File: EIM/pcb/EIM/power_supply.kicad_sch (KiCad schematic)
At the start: 18 parts, among them U2 AP63203WU, U6 AP63200WU

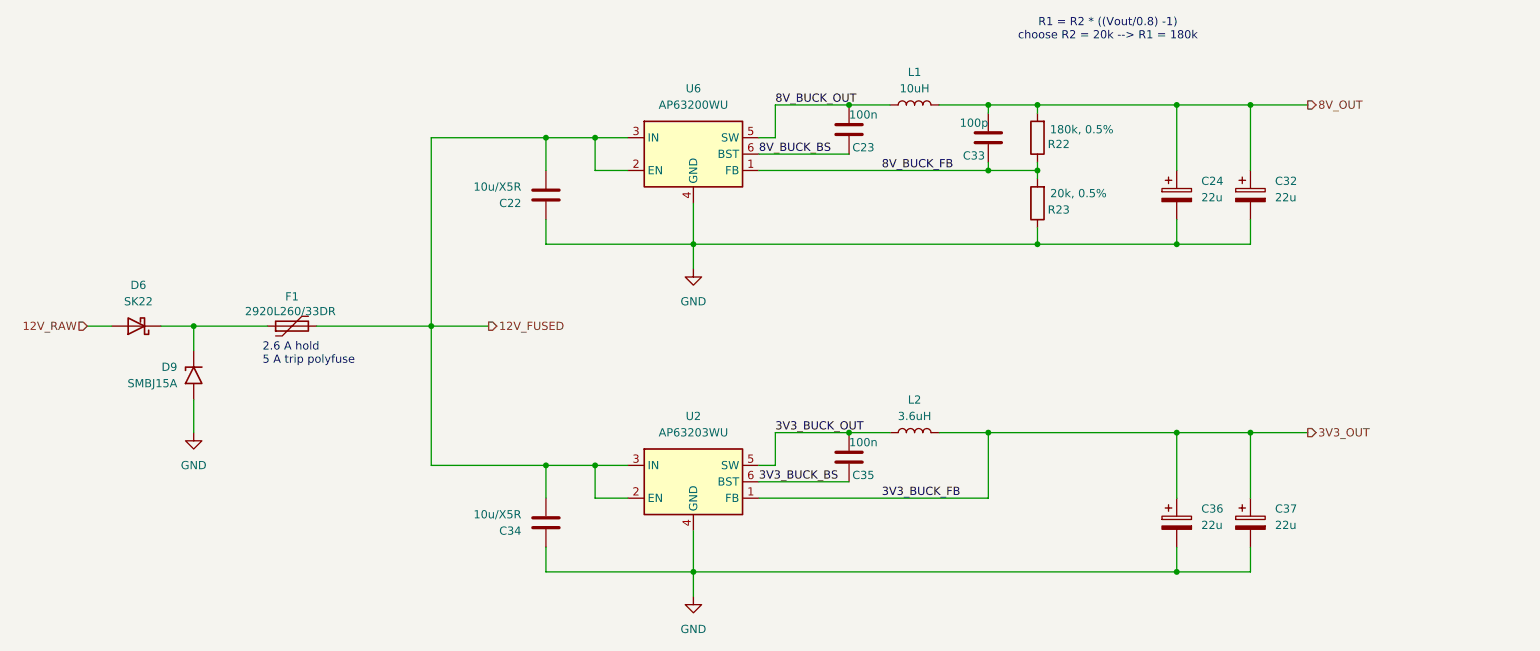
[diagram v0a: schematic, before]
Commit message: added Arjun's comments, assigned some MCU pins
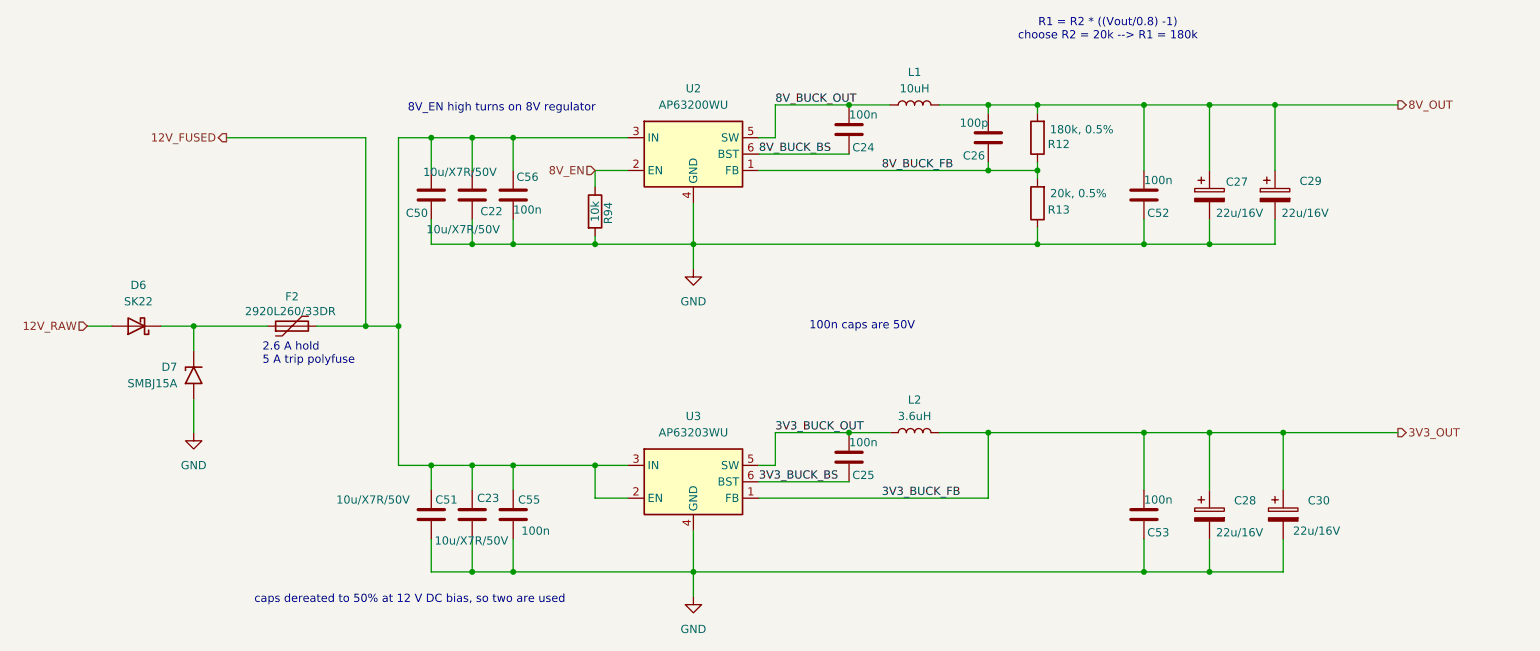
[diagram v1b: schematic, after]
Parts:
- added C50, C51: 10u/X7R/50V, Capacitor_SMD:C_1206_3216Metric_Pad1.33x1.80mm_HandSolder, symbol Device:C
- added C52, C53, C55, C56: 100n, Capacitor_SMD:C_0805_2012Metric_Pad1.18x1.45mm_HandSolder, symbol Device:C
- added R94: 10k, Resistor_SMD:R_0805_2012Metric_Pad1.20x1.40mm_HandSolder, symbol Device:R
- C22: value 10u/X5R -> 10u/X7R/50V
- C23: renamed from C34; value 10u/X5R -> 10u/X7R/50V
- C27: renamed from C24; value 22u -> 22u/16V
- C28: renamed from C36; value 22u -> 22u/16V
- C29: renamed from C32; value 22u -> 22u/16V
- C30: renamed from C37; value 22u -> 22u/16V
- renumbered C23 to C24, C35 to C25, C33 to C26, D9 to D7, F1 to F2, R22 to R12, R23 to R13, U6 to U2, U2 to U3
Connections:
- net 12V_FUSED: now also C50.1, C51.2, C55.1, C56.2; no longer U2.2 (EN)
- net 3V3_OUT: now also C53.1
- net 8V_OUT: now also C52.1
- net GND: now also C50.2, C51.1, C52.2, C53.2, C55.2, C56.1, R94.2
- new net 8V_EN: R94.1, U2.2 (EN)
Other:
- note added: "100n caps are 50V"
- note added: "8V_EN high turns on 8V regulator"
- note added: "caps dereated to 50% at 12 V DC bias, so two are used"
- moved on the sheet: C22, C23, C27, C28, C29, C30

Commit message: Layout 75% done, before 8V bus deletion
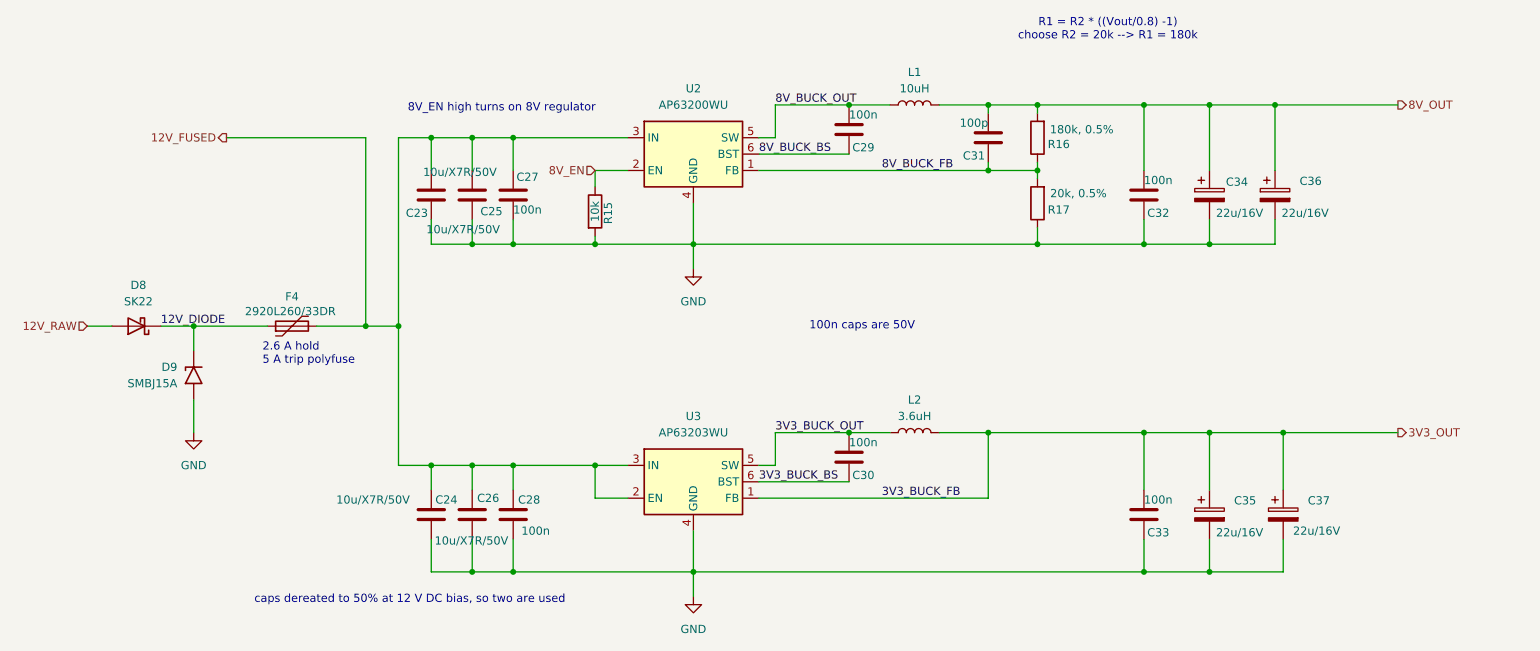
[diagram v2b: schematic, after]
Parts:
- renumbered C50 to C23, C51 to C24, C22 to C25, C23 to C26, C56 to C27, C55 to C28, C24 to C29, C25 to C30, C26 to C31, C52 to C32, C53 to C33, C27 to C34, C28 to C35, C29 to C36, C30 to C37, D6 to D8, D7 to D9, F2 to F4, R94 to R15, R12 to R16, R13 to R17
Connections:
- net 12V_DIODE: now reaches D8.1 (K), D9.1 (A1), F4.1
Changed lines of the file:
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@@
+		)
+	)
+	(label "12V_DIODE"
+		(at 50.8 95.25 0)
+		(fields_autoplaced yes)
+		(effects
+			(font
+				(size 1.27 1.27)
+			)
+			(justify left bottom)
 		)
 	)
@@
 		(on_board yes)
 		(dnp no)
-		(property "Reference" "C55"
+		(property "Reference" "C28"
 			(at 106.172 122.174 0)
 			(effects
@@
 			(project "EIM"
 				(path "/2e0b3b3d-5537-41dc-9fad-4fb33afdbfad/dc39c068-2af2-4b70-9a5c-946b676fc222"
-					(reference "C55")
+					(reference "C28")
 					(unit 1)
 				)
@@
 		(on_board yes)
 		(dnp no)
-		(property "Reference" "C50"
+		(property "Reference" "C23"
 			(at 92.202 77.724 0)
 			(effects
@@
 			(project "EIM"
 				(path "/2e0b3b3d-5537-41dc-9fad-4fb33afdbfad/dc39c068-2af2-4b70-9a5c-946b676fc222"
-					(reference "C50")
+					(reference "C23")
 					(unit 1)
 				)
@@
 		(on_board yes)
 		(dnp no)
-		(property "Reference" "C56"
+		(property "Reference" "C27"
 			(at 105.918 72.136 0)
 			(effects
@@
 			(project "EIM"
 				(path "/2e0b3b3d-5537-41dc-9fad-4fb33afdbfad/dc39c068-2af2-4b70-9a5c-946b676fc222"
-					(reference "C56")
+					(reference "C27")
 					(unit 1)
 				)
@@
 		(on_board yes)
 		(dnp no)
-		(property "Reference" "C26"
+		(property "Reference" "C31"
 			(at 178.562 68.834 0)
 			(effects
@@
 			(project "EIM"
 				(path "/2e0b3b3d-5537-41dc-9fad-4fb33afdbfad/dc39c068-2af2-4b70-9a5c-946b676fc222"
-					(reference "C26")
+					(reference "C31")
 					(unit 1)
 				)
@@
 		(on_board yes)
 		(dnp no)
-		(property "Reference" "C28"
+		(property "Reference" "C35"
 			(at 217.17 122.3009 0)
 			(effects
@@
 			(project "EIM"
 				(path "/2e0b3b3d-5537-41dc-9fad-4fb33afdbfad/dc39c068-2af2-4b70-9a5c-946b676fc222"
-					(reference "C28")
+					(reference "C35")
 					(unit 1)
 				)
@@
 		(on_board yes)
 		(dnp no)
-		(property "Reference" "R94"
+		(property "Reference" "R15"
 			(at 120.142 77.724 90)
 			(effects
@@
 			(project "EIM"
 				(path "/2e0b3b3d-5537-41dc-9fad-4fb33afdbfad/dc39c068-2af2-4b70-9a5c-946b676fc222"
-					(reference "R94")
+					(reference "R15")
 					(unit 1)
 				)
@@
 		(on_board yes)
 		(dnp no)
-		(property "Reference" "C24"
+		(property "Reference" "C29"
 			(at 157.988 67.564 0)
 			(effects
@@
 			(project "EIM"
 				(path "/2e0b3b3d-5537-41dc-9fad-4fb33afdbfad/dc39c068-2af2-4b70-9a5c-946b676fc222"
-					(reference "C24")
+					(reference "C29")
 					(unit 1)
 				)
@@
 		(on_board yes)
 		(dnp no)
-		(property "Reference" "C29"
+		(property "Reference" "C36"
 			(at 227.33 72.7709 0)
 			(effects
@@
 			(project "EIM"
 				(path "/2e0b3b3d-5537-41dc-9fad-4fb33afdbfad/dc39c068-2af2-4b70-9a5c-946b676fc222"
-					(reference "C29")
+					(reference "C36")
 					(unit 1)
 				)
@@
 		(on_board yes)
 		(dnp no)
-		(property "Reference" "C52"
+		(property "Reference" "C32"
 			(at 203.708 77.724 0)
 			(effects
@@
 			(project "EIM"
 				(path "/2e0b3b3d-5537-41dc-9fad-4fb33afdbfad/dc39c068-2af2-4b70-9a5c-946b676fc222"
-					(reference "C52")
+					(reference "C32")
 					(unit 1)
 				)
@@
 		(on_board yes)
 		(dnp no)
-		(property "Reference" "C25"
+		(property "Reference" "C30"
 			(at 157.988 118.364 0)
 			(effects
@@
 			(project "EIM"
 				(path "/2e0b3b3d-5537-41dc-9fad-4fb33afdbfad/dc39c068-2af2-4b70-9a5c-946b676fc222"
-					(reference "C25")
+					(reference "C30")
 					(unit 1)
 				)
@@
 		(dnp no)
 		(fields_autoplaced yes)
-		(property "Reference" "#PWR067"
+		(property "Reference" "#PWR076"
 			(at 133.35 143.51 0)
 			(effects
@@
 			(project "EIM"
 				(path "/2e0b3b3d-5537-41dc-9fad-4fb33afdbfad/dc39c068-2af2-4b70-9a5c-946b676fc222"
-					(reference "#PWR067")
+					(reference "#PWR076")
 					(unit 1)
 				)
@@
 		(dnp no)
 		(fields_autoplaced yes)
-		(property "Reference" "D6"
+		(property "Reference" "D8"
 			(at 47.3075 88.9 0)
 			(effects
@@
 			(project ""
 				(path "/2e0b3b3d-5537-41dc-9fad-4fb33afdbfad/dc39c068-2af2-4b70-9a5c-946b676fc222"
-					(reference "D6")
+					(reference "D8")
 					(unit 1)
 				)
@@
 		(dnp no)
 		(fields_autoplaced yes)
-		(property "Reference" "#PWR066"
+		(property "Reference" "#PWR075"
 			(at 133.35 92.71 0)
 			(effects
@@
 			(project "EIM"
 				(path "/2e0b3b3d-5537-41dc-9fad-4fb33afdbfad/dc39c068-2af2-4b70-9a5c-946b676fc222"
-					(reference "#PWR066")
+					(reference "#PWR075")
 					(unit 1)
 				)
@@
 		(on_board yes)
 		(dnp no)
-		(property "Reference" "C51"
+		(property "Reference" "C24"
 			(at 96.774 122.174 0)
 			(effects
@@
 			(project "EIM"
 				(path "/2e0b3b3d-5537-41dc-9fad-4fb33afdbfad/dc39c068-2af2-4b70-9a5c-946b676fc222"
-					(reference "C51")
+					(reference "C24")
 					(unit 1)
 				)
@@
 		(on_board yes)
 		(dnp no)
-		(property "Reference" "D7"
+		(property "Reference" "D9"
 			(at 53.34 101.5999 90)
 			(effects
@@
 			(project "EIM"
 				(path "/2e0b3b3d-5537-41dc-9fad-4fb33afdbfad/dc39c068-2af2-4b70-9a5c-946b676fc222"
-					(reference "D7")
+					(reference "D9")
 					(unit 1)
 				)
@@
 		(on_board yes)
 		(dnp no)
-		(property "Reference" "C22"
+		(property "Reference" "C25"
 			(at 100.33 77.47 0)
 			(effects
@@
 			(project "EIM"
 				(path "/2e0b3b3d-5537-41dc-9fad-4fb33afdbfad/dc39c068-2af2-4b70-9a5c-946b676fc222"
-					(reference "C22")
+					(reference "C25")
 					(unit 1)
 				)
@@
 		(on_board yes)
 		(dnp no)
-		(property "Reference" "C30"
+		(property "Reference" "C37"
 			(at 228.6 122.3009 0)
 			(effects
@@
 			(project "EIM"
 				(path "/2e0b3b3d-5537-41dc-9fad-4fb33afdbfad/dc39c068-2af2-4b70-9a5c-946b676fc222"
-					(reference "C30")
+					(reference "C37")
 					(unit 1)
 				)
@@
 		(on_board yes)
 		(dnp no)
-		(property "Reference" "C53"
+		(property "Reference" "C33"
 			(at 203.708 127.254 0)
 			(effects
@@
 			(project "EIM"
 				(path "/2e0b3b3d-5537-41dc-9fad-4fb33afdbfad/dc39c068-2af2-4b70-9a5c-946b676fc222"
-					(reference "C53")
+					(reference "C33")
 					(unit 1)
 				)
@@
 		(dnp no)
 		(fields_autoplaced yes)
-		(property "Reference" "#PWR065"
+		(property "Reference" "#PWR074"
 			(at 55.88 118.11 0)
 			(effects
@@
 			(project "EIM"
 				(path "/2e0b3b3d-5537-41dc-9fad-4fb33afdbfad/dc39c068-2af2-4b70-9a5c-946b676fc222"
-					(reference "#PWR065")
+					(reference "#PWR074")
 					(unit 1)
 				)
@@
 		(on_board yes)
 		(dnp no)
-		(property "Reference" "R12"
+		(property "Reference" "R16"
 			(at 189.992 67.056 0)
 			(effects
@@
 			(project "EIM"
 				(path "/2e0b3b3d-5537-41dc-9fad-4fb33afdbfad/dc39c068-2af2-4b70-9a5c-946b676fc222"
-					(reference "R12")
+					(reference "R16")
 					(unit 1)
 				)
@@
 		(on_board yes)
 		(dnp no)
-		(property "Reference" "F2"
+		(property "Reference" "F4"
 			(at 71.12 90.678 90)
 			(effects
@@
 			(project "EIM"
 				(path "/2e0b3b3d-5537-41dc-9fad-4fb33afdbfad/dc39c068-2af2-4b70-9a5c-946b676fc222"
-					(reference "F2")
+					(reference "F4")
 					(unit 1)
 				)
@@
 		(on_board yes)
 		(dnp no)
-		(property "Reference" "C27"
+		(property "Reference" "C34"
 			(at 215.9 72.898 0)
 			(effects
@@
 			(project ""
 				(path "/2e0b3b3d-5537-41dc-9fad-4fb33afdbfad/dc39c068-2af2-4b70-9a5c-946b676fc222"
-					(reference "C27")
+					(reference "C34")
 					(unit 1)
 				)
@@
 		(on_board yes)
 		(dnp no)
-		(property "Reference" "R13"
+		(property "Reference" "R17"
 			(at 189.992 77.216 0)
 			(effects
@@
 			(project "EIM"
 				(path "/2e0b3b3d-5537-41dc-9fad-4fb33afdbfad/dc39c068-2af2-4b70-9a5c-946b676fc222"
-					(reference "R13")
+					(reference "R17")
 					(unit 1)
 				)
@@
 		(on_board yes)
 		(dnp no)
-		(property "Reference" "C23"
+		(property "Reference" "C26"
 			(at 99.822 121.92 0)
 			(effects
@@
 			(project "EIM"
 				(path "/2e0b3b3d-5537-41dc-9fad-4fb33afdbfad/dc39c068-2af2-4b70-9a5c-946b676fc222"
-					(reference "C23")
-					(unit 1)
-				)
+					(reference "C26")
+					(unit 1)
+				)

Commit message: All components placed and pins assigned.
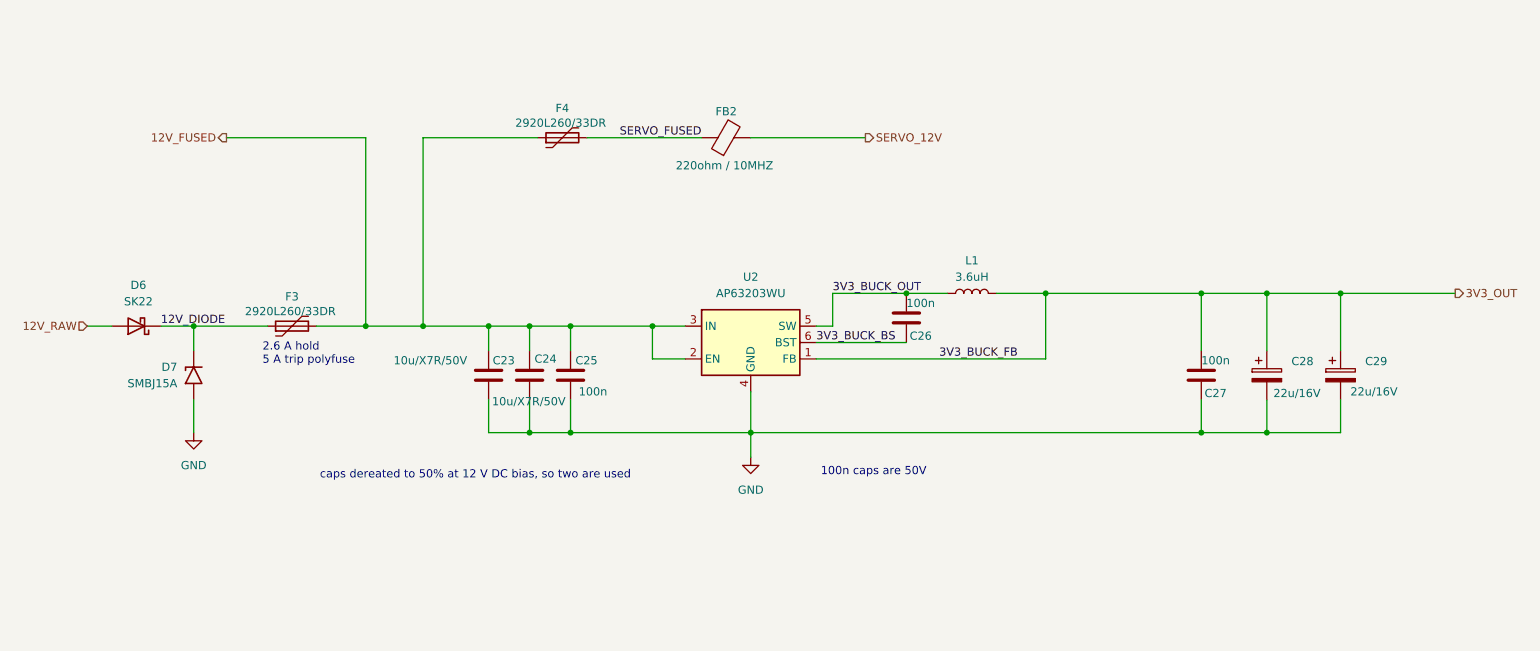
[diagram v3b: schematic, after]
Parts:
- removed C23, C25: 10u/X7R/50V, Capacitor_SMD:C_1206_3216Metric_Pad1.33x1.80mm_HandSolder, symbol Device:C
- removed C27, C29, C32: 100n, Capacitor_SMD:C_0805_2012Metric_Pad1.18x1.45mm_HandSolder, symbol Device:C
- removed C31: 100p, Capacitor_SMD:C_0805_2012Metric_Pad1.18x1.45mm_HandSolder, symbol Device:C
- removed C34, C36: 22u/16V, Capacitor_SMD:CP_Elec_4x5.8, symbol Device:C_Polarized
- removed L1: 10uH, Inductor_SMD:L_Bourns-SRN8040_8x8.15mm, symbol Device:L
- removed R15: 10k, Resistor_SMD:R_0805_2012Metric_Pad1.20x1.40mm_HandSolder, symbol Device:R
- removed R16: 180k, 0.5%, Resistor_SMD:R_0805_2012Metric_Pad1.20x1.40mm_HandSolder, symbol Device:R
- removed R17: 20k, 0.5%, Resistor_SMD:R_0805_2012Metric_Pad1.20x1.40mm_HandSolder, symbol Device:R
- removed U2: AP63200WU, Package_TO_SOT_SMD:TSOT-23-6, symbol Regulator_Switching:AP63200WU
- added F4: 2920L260/33DR, Fuse:Fuse_2920_7451Metric, symbol Device:Polyfuse
- added FB2: 220ohm / 10MHZ, Inductor_SMD:L_0805_2012Metric_Pad1.15x1.40mm_HandSolder, symbol Device:FerriteBead
- D6: renamed from D8; footprint Diode_SMD:D_SMB_Handsoldering -> Diode_SMD:D_SMB
- renumbered C24 to C23, C26 to C24, C28 to C25, C30 to C26, C33 to C27, C35 to C28, C37 to C29, D9 to D7, F4 to F3, L2 to L1, U3 to U2
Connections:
- net 12V_FUSED: now also F4.1
- new net SERVO_12V: FB2.2
- new net SERVO_FUSED: F4.2, FB2.1
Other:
- note removed: "8V_EN high turns on 8V regulator"
- note removed: "R1 = R2 * ((Vout/0.8) -1) choose R2 = 20k --> R1 = 180k"
- moved on the sheet: C23, C24, C25, C26, C27, C28, C29, L1, U2
